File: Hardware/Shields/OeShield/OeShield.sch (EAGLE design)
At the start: 15 parts, among them IC2 MAX3082

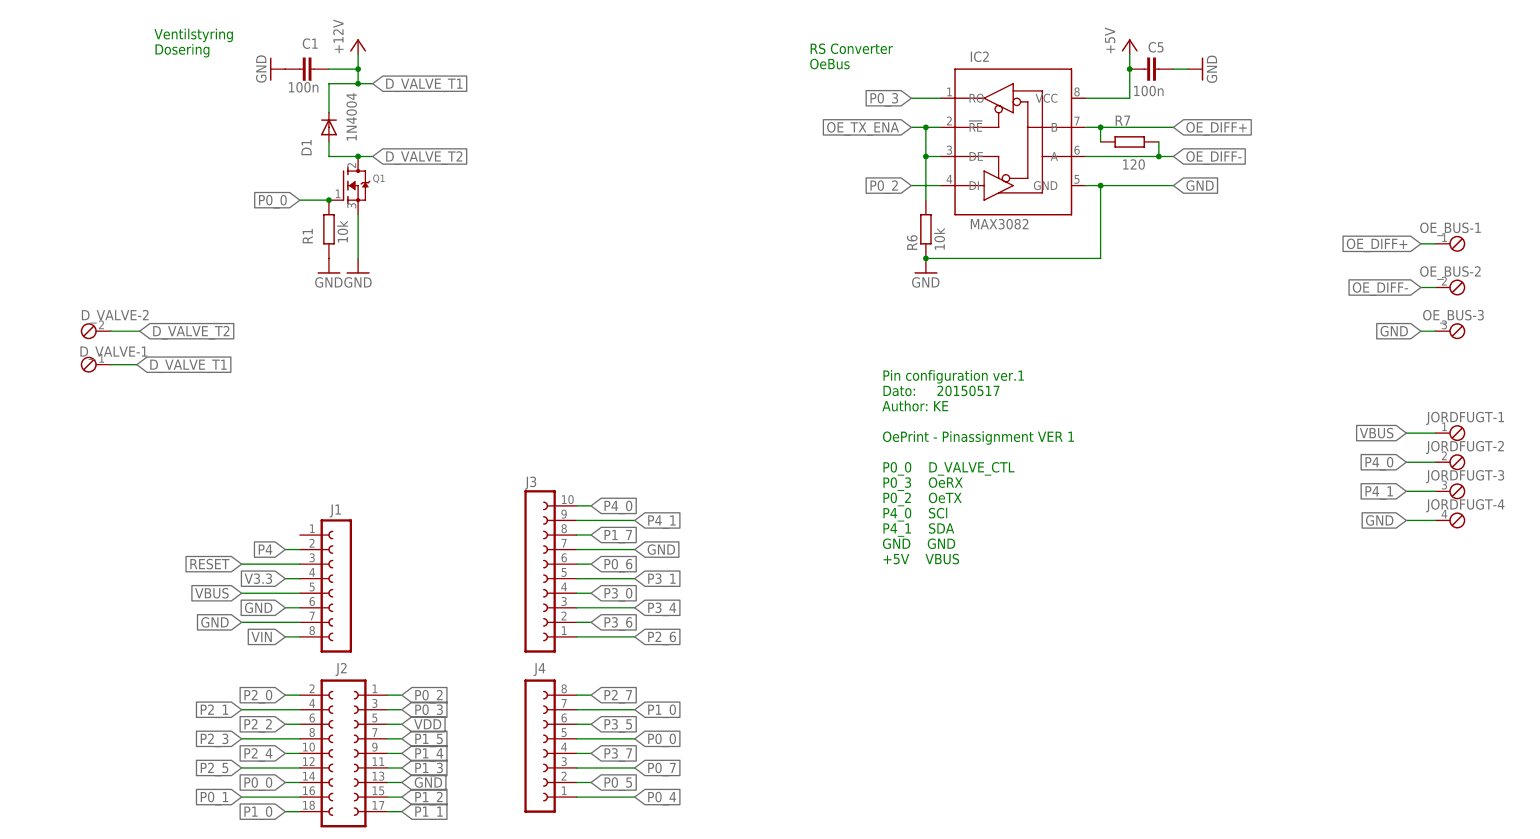
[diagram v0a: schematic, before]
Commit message: Shields pin_update KE
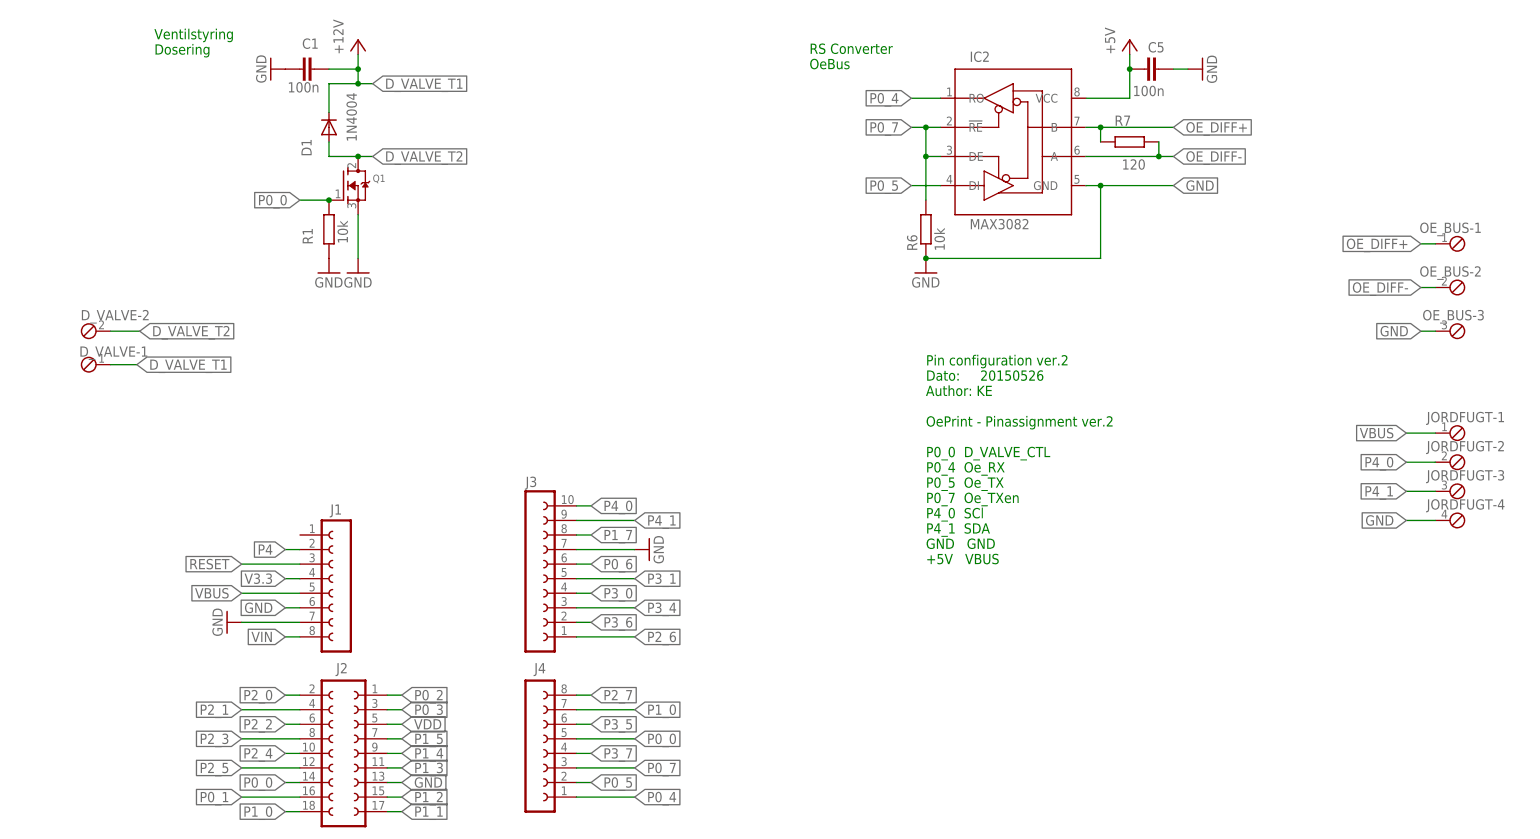
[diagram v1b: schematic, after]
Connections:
- removed net OE_TX_ENA: IC2.!RE!, IC2.DE, R6.2
- net P0_2: no longer IC2.DI
- net P0_3: no longer IC2.RO
- net P0_4: now also IC2.RO
- net P0_5: now also IC2.DI
- net P0_7: now also IC2.!RE!, IC2.DE, R6.2
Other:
- note added: "Pin configuration ver.2 Dato: 20150526 Author: KE OePrint - Pinassignment ver.2 P0_0 D_VALVE_CTL P0_4 Oe_RX P0_5 Oe_TX P0_7 Oe_TXen P4_0 SCl P4_1 SDA GND GND +5V VBUS"
- note removed: "Pin configuration ver.1 Dato: 20150517 Author: KE OePrint - Pinassignment VER 1 P0_0 D_VALVE_CTL P0_3 OeRX P0_2 OeTX P4_0 SCl P4_1 SDA GND GND +5V VBUS"

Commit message: Bilag added KE
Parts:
- added +12V: (no value), con-phoenix-254:MPT2
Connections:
- net GND: now also +12V-1.1
- net VCC: now also +12V-2.1
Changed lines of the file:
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@@
 <part name="GND1" library="supply1" deviceset="GND" device=""/>
 <part name="GND3" library="supply1" deviceset="GND" device=""/>
+<part name="+12V" library="con-phoenix-254" deviceset="MPT2" device=""/>
+<part name="P+2" library="supply1" deviceset="VCC" device="" value="+12V"/>
 </parts>
 <sheets>
@@
 Dosering</text>
 <text x="73.66" y="20.32" size="1.778" layer="91">Pin configuration ver.2
-Dato: 	20150526
+Dato:  20150526
 Author: KE
 OePrint - Pinassignment ver.2
@@
 <instance part="GND1" gate="1" x="-48.26" y="10.16" rot="R270"/>
 <instance part="GND3" gate="1" x="25.4" y="22.86" rot="R90"/>
+<instance part="+12V" gate="-1" x="-71.12" y="33.02" rot="R180"/>
+<instance part="+12V" gate="-2" x="-71.12" y="38.1" rot="R180"/>
+<instance part="P+2" gate="VCC" x="-60.96" y="38.1" rot="R270"/>
 </instances>
 <busses>
@@
 <label x="157.48" y="27.94" size="1.778" layer="95" rot="R180" xref="yes"/>
 </segment>
+<segment>
+<pinref part="+12V" gate="-1" pin="1"/>
+<wire x1="-68.58" y1="33.02" x2="-63.5" y2="33.02" width="0.1524" layer="91"/>
+<label x="-63.5" y="33.02" size="1.778" layer="95" xref="yes"/>
+</segment>
 </net>
 <net name="P0_1" class="0">
@@
 <junction x="109.22" y="106.68"/>
 </segment>
+<segment>
+<pinref part="+12V" gate="-2" pin="1"/>
+<wire x1="-68.58" y1="38.1" x2="-63.5" y2="38.1" width="0.1524" layer="91"/>
+<pinref part="P+2" gate="VCC" pin="VCC"/>
+</segment>
 </net>

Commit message: Shields KE
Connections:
- removed net VCC: +12V-2.1, C5.1, IC2.VCC
- net D_VALVE_T1: now also +12V-2.1, C5.1, IC2.VCC
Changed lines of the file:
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@@
 <parts>
 <part name="Q1" library="adafruit" deviceset="MOSFET-N" device="GDS_TO220V"/>
-<part name="GND2" library="supply1" deviceset="GND" device=""/>
-<part name="GND6" library="supply1" deviceset="GND" device=""/>
-<part name="P+1" library="supply1" deviceset="VCC" device="" value="+12V"/>
 <part name="D1" library="adafruit" deviceset="1N4004" device=""/>
 <part name="FRAME1" library="frames" deviceset="A4L-LOC" device=""/>
@@
 <part name="IC2" library="myLibrary" deviceset="MAX3082" device="CPD" value="MAX3082"/>
 <part name="R6" library="resistor" deviceset="R-EU_" device="0207/12" value="10k"/>
-<part name="P+5" library="supply1" deviceset="VCC" device="" value="+5V"/>
 <part name="R7" library="resistor" deviceset="R-EU_" device="0207/12" value="120"/>
 <part name="C5" library="capacitor-wima" deviceset="C" device="5/3" value="100n"/>
 <part name="GND11" library="supply1" deviceset="GND" device=""/>
 <part name="R1" library="resistor" deviceset="R-EU_" device="0207/12" value="10k"/>
-<part name="GND16" library="supply1" deviceset="GND" device=""/>
 <part name="OE_BUS" library="con-phoenix-254" deviceset="MPT3" device=""/>
 <part name="D_VALVE" library="con-phoenix-254" deviceset="MPT2" device=""/>
@@
 <part name="J1" library="con-lsta" deviceset="FE08-1" device=""/>
 <part name="JORDFUGT" library="con-phoenix-254" deviceset="MPT4" device=""/>
-<part name="GND1" library="supply1" deviceset="GND" device=""/>
 <part name="GND3" library="supply1" deviceset="GND" device=""/>
 <part name="+12V" library="con-phoenix-254" deviceset="MPT2" device=""/>
-<part name="P+2" library="supply1" deviceset="VCC" device="" value="+12V"/>
 </parts>
 <sheets>
@@
 <instances>
 <instance part="Q1" gate="G$1" x="-27.94" y="86.36"/>
-<instance part="GND2" gate="1" x="-25.4" y="71.12"/>
-<instance part="GND6" gate="1" x="-30.48" y="71.12"/>
-<instance part="P+1" gate="VCC" x="-25.4" y="111.76"/>
 <instance part="D1" gate="1" x="-30.48" y="96.52" smashed="yes" rot="R90">
 <attribute name="NAME" x="-33.5026" y="91.44" size="1.778" layer="95" rot="R90"/>
@@
 <instance part="IC2" gate="G$1" x="88.9" y="93.98"/>
 <instance part="R6" gate="G$1" x="73.66" y="78.74" rot="R90"/>
-<instance part="P+5" gate="VCC" x="109.22" y="111.76"/>
 <instance part="R7" gate="G$1" x="109.22" y="93.98" smashed="yes" rot="R180">
 <attribute name="NAME" x="109.474" y="98.5774" size="1.778" layer="95" rot="R180"/>
@@
 <attribute name="VALUE" x="-28.956" y="80.264" size="1.778" layer="96" rot="R270"/>
 </instance>
-<instance part="GND16" gate="1" x="73.66" y="71.12"/>
 <instance part="OE_BUS" gate="-1" x="165.1" y="76.2" smashed="yes">
 <attribute name="NAME" x="159.766" y="78.105" size="1.778" layer="95"/>
@@
 <attribute name="VALUE" x="164.084" y="24.638" size="1.778" layer="96"/>
 </instance>
-<instance part="GND1" gate="1" x="-48.26" y="10.16" rot="R270"/>
 <instance part="GND3" gate="1" x="25.4" y="22.86" rot="R90"/>
 <instance part="+12V" gate="-1" x="-71.12" y="33.02" rot="R180"/>
 <instance part="+12V" gate="-2" x="-71.12" y="38.1" rot="R180"/>
-<instance part="P+2" gate="VCC" x="-60.96" y="38.1" rot="R270"/>
 </instances>
 <busses>
@@
 <net name="GND" class="0">
 <segment>
-<pinref part="Q1" gate="G$1" pin="S"/>
-<pinref part="GND2" gate="1" pin="GND"/>
-<wire x1="-25.4" y1="73.66" x2="-25.4" y2="81.28" width="0.1524" layer="91"/>
-</segment>
-<segment>
 <pinref part="C1" gate="G$1" pin="2"/>
 <pinref part="GND7" gate="1" pin="GND"/>
@@
 </segment>
 <segment>
-<pinref part="GND6" gate="1" pin="GND"/>
+<pinref part="J3" gate="G$1" pin="7"/>
+<wire x1="22.86" y1="22.86" x2="12.7" y2="22.86" width="0.1524" layer="91"/>
+<pinref part="GND3" gate="1" pin="GND"/>
+</segment>
+<segment>
+<label x="-38.1" y="12.7" size="1.778" layer="95" rot="R180" xref="yes"/>
+<pinref part="J1" gate="G$1" pin="6"/>
+<wire x1="-35.56" y1="12.7" x2="-38.1" y2="12.7" width="0.1524" layer="91"/>
+</segment>
+<segment>
+<pinref part="J2" gate="1" pin="13"/>
+<wire x1="-20.32" y1="-17.78" x2="-17.78" y2="-17.78" width="0.1524" layer="91"/>
+<label x="-17.78" y="-17.78" size="1.778" layer="95" xref="yes"/>
+</segment>
+<segment>
+<pinref part="JORDFUGT" gate="-4" pin="1"/>
+<wire x1="162.56" y1="27.94" x2="104.14" y2="27.94" width="0.1524" layer="91"/>
+<pinref part="OE_BUS" gate="-3" pin="1"/>
+<wire x1="162.56" y1="60.96" x2="104.14" y2="60.96" width="0.1524" layer="91"/>
+<pinref part="+12V" gate="-1" pin="1"/>
+<wire x1="-68.58" y1="33.02" x2="-63.5" y2="33.02" width="0.1524" layer="91"/>
+<label x="-63.5" y="33.02" size="1.778" layer="95" xref="yes"/>
+<pinref part="J1" gate="G$1" pin="7"/>
+<wire x1="-35.56" y1="10.16" x2="-63.5" y2="10.16" width="0.1524" layer="91"/>
+<wire x1="-63.5" y1="10.16" x2="-63.5" y2="33.02" width="0.1524" layer="91"/>
+<wire x1="-63.5" y1="33.02" x2="-30.48" y2="33.02" width="0.1524" layer="91"/>
+<wire x1="-30.48" y1="33.02" x2="-30.48" y2="71.12" width="0.1524" layer="91"/>
 <pinref part="R1" gate="G$1" pin="2"/>
-</segment>
-<segment>
+<pinref part="Q1" gate="G$1" pin="S"/>
+<wire x1="-30.48" y1="71.12" x2="-30.48" y2="73.66" width="0.1524" layer="91"/>
+<wire x1="-25.4" y1="73.66" x2="-25.4" y2="81.28" width="0.1524" layer="91"/>
+<wire x1="-25.4" y1="73.66" x2="-30.48" y2="71.12" width="0.1524" layer="91"/>
+<junction x="-30.48" y="71.12"/>
 <pinref part="R6" gate="G$1" pin="1"/>
 <wire x1="73.66" y1="73.66" x2="104.14" y2="73.66" width="0.1524" layer="91"/>
@@
 <label x="116.84" y="86.36" size="1.778" layer="95" xref="yes"/>
 <junction x="104.14" y="86.36"/>
-<pinref part="GND16" gate="1" pin="GND"/>
-<junction x="73.66" y="73.66"/>
-</segment>
-<segment>
-<pinref part="J3" gate="G$1" pin="7"/>
-<wire x1="22.86" y1="22.86" x2="12.7" y2="22.86" width="0.1524" layer="91"/>
-<pinref part="GND3" gate="1" pin="GND"/>
-</segment>
-<segment>
-<pinref part="J1" gate="G$1" pin="7"/>
-<wire x1="-35.56" y1="10.16" x2="-45.72" y2="10.16" width="0.1524" layer="91"/>
-<pinref part="GND1" gate="1" pin="GND"/>
-</segment>
-<segment>
-<label x="-38.1" y="12.7" size="1.778" layer="95" rot="R180" xref="yes"/>
-<pinref part="J1" gate="G$1" pin="6"/>
-<wire x1="-35.56" y1="12.7" x2="-38.1" y2="12.7" width="0.1524" layer="91"/>
-</segment>
-<segment>
-<pinref part="OE_BUS" gate="-3" pin="1"/>
-<wire x1="162.56" y1="60.96" x2="160.02" y2="60.96" width="0.1524" layer="91"/>
-<label x="160.02" y="60.96" size="1.778" layer="95" rot="R180" xref="yes"/>
-</segment>
-<segment>
-<pinref part="J2" gate="1" pin="13"/>
-<wire x1="-20.32" y1="-17.78" x2="-17.78" y2="-17.78" width="0.1524" layer="91"/>
-<label x="-17.78" y="-17.78" size="1.778" layer="95" xref="yes"/>
-</segment>
-<segment>
-<pinref part="JORDFUGT" gate="-4" pin="1"/>
-<wire x1="162.56" y1="27.94" x2="157.48" y2="27.94" width="0.1524" layer="91"/>
-<label x="157.48" y="27.94" size="1.778" layer="95" rot="R180" xref="yes"/>
-</segment>
-<segment>
-<pinref part="+12V" gate="-1" pin="1"/>
-<wire x1="-68.58" y1="33.02" x2="-63.5" y2="33.02" width="0.1524" layer="91"/>
-<label x="-63.5" y="33.02" size="1.778" layer="95" xref="yes"/>
+<wire x1="73.66" y1="73.66" x2="-25.4" y2="73.66" width="0.1524" layer="91"/>
+<junction x="-25.4" y="73.66"/>
+<wire x1="104.14" y1="60.96" x2="104.14" y2="73.66" width="0.1524" layer="91"/>
+<junction x="104.14" y="73.66"/>
+<wire x1="104.14" y1="27.94" x2="104.14" y2="60.96" width="0.1524" layer="91"/>
+<junction x="104.14" y="60.96"/>
 </segment>
 </net>
@@
 <wire x1="-35.56" y1="-20.32" x2="-45.72" y2="-20.32" width="0.1524" layer="91"/>
 <label x="-45.72" y="-20.32" size="1.778" layer="95" rot="R180" xref="yes"/>
-</segment>
-</net>
-<net name="VCC" class="0">
-<segment>
-<pinref part="IC2" gate="G$1" pin="VCC"/>
-<wire x1="101.6" y1="101.6" x2="109.22" y2="101.6" width="0.1524" layer="91"/>
-<pinref part="P+5" gate="VCC" pin="VCC"/>
-<wire x1="109.22" y1="109.22" x2="109.22" y2="106.68" width="0.1524" layer="91"/>
-<pinref part="C5" gate="G$1" pin="1"/>
-<wire x1="109.22" y1="106.68" x2="109.22" y2="101.6" width="0.1524" layer="91"/>
-<junction x="109.22" y="106.68"/>
-</segment>
-<segment>
-<pinref part="+12V" gate="-2" pin="1"/>
-<wire x1="-68.58" y1="38.1" x2="-63.5" y2="38.1" width="0.1524" layer="91"/>
-<pinref part="P+2" gate="VCC" pin="VCC"/>
 </segment>
 </net>
@@
 <label x="-22.86" y="104.14" size="1.778" layer="95" xref="yes"/>
 <wire x1="-22.86" y1="104.14" x2="-25.4" y2="104.14" width="0.1524" layer="91"/>
-<pinref part="P+1" gate="VCC" pin="VCC"/>
 <wire x1="-30.48" y1="104.14" x2="-25.4" y2="104.14" width="0.1524" layer="91"/>
 <wire x1="-25.4" y1="104.14" x2="-25.4" y2="106.68" width="0.1524" layer="91"/>
 <junction x="-25.4" y="104.14"/>
-<wire x1="-25.4" y1="106.68" x2="-25.4" y2="109.22" width="0.1524" layer="91"/>
 <wire x1="-25.4" y1="106.68" x2="-30.48" y2="106.68" width="0.1524" layer="91"/>
 <pinref part="C1" gate="G$1" pin="1"/>
 <junction x="-25.4" y="106.68"/>
-</segment>
-</net>
+<wire x1="-25.4" y1="106.68" x2="-25.4" y2="114.3" width="0.1524" layer="91"/>
+<wire x1="-25.4" y1="114.3" x2="20.32" y2="114.3" width="0.1524" layer="91"/>
+<wire x1="20.32" y1="114.3" x2="20.32" y2="93.98" width="0.1524" layer="91"/>
+<pinref part="IC2" gate="G$1" pin="VCC"/>
+<wire x1="20.32" y1="93.98" x2="20.32" y2="91.44" width="0.1524" layer="91"/>
+<wire x1="101.6" y1="101.6" x2="109.22" y2="101.6" width="0.1524" layer="91"/>
+<pinref part="C5" gate="G$1" pin="1"/>
+<wire x1="109.22" y1="106.68" x2="109.22" y2="101.6" width="0.1524" layer="91"/>
+<junction x="109.22" y="106.68"/>
+<wire x1="109.22" y1="106.68" x2="109.22" y2="114.3" width="0.1524" layer="91"/>
+<wire x1="109.22" y1="114.3" x2="20.32" y2="114.3" width="0.1524" layer="91"/>
+<pinref part="+12V" gate="-2" pin="1"/>
+<wire x1="-68.58" y1="38.1" x2="20.32" y2="38.1" width="0.1524" layer="91"/>
+<wire x1="20.32" y1="38.1" x2="20.32" y2="91.44" width="0.1524" layer="91"/>
+</segment>
+</net>
